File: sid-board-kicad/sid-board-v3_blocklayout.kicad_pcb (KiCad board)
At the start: 2 copper layers, 49 parts, among them J1 SPI + UART, J2 USB_B_Micro, J3 UART, Q1 BSS138, Q2 BSS138, SW1 SW_EN, SW2 SW_FLASH, U1 SC16IS752IPW, U2 MCP1703A-3302_SOT223, U3 SN65HVD232, U4 SN65HVD232, U5 CY7C65213-28PVXI, U6 ESP32-WROOM-32U, U7 SN65HVD232, X1 S53305-24.000-X

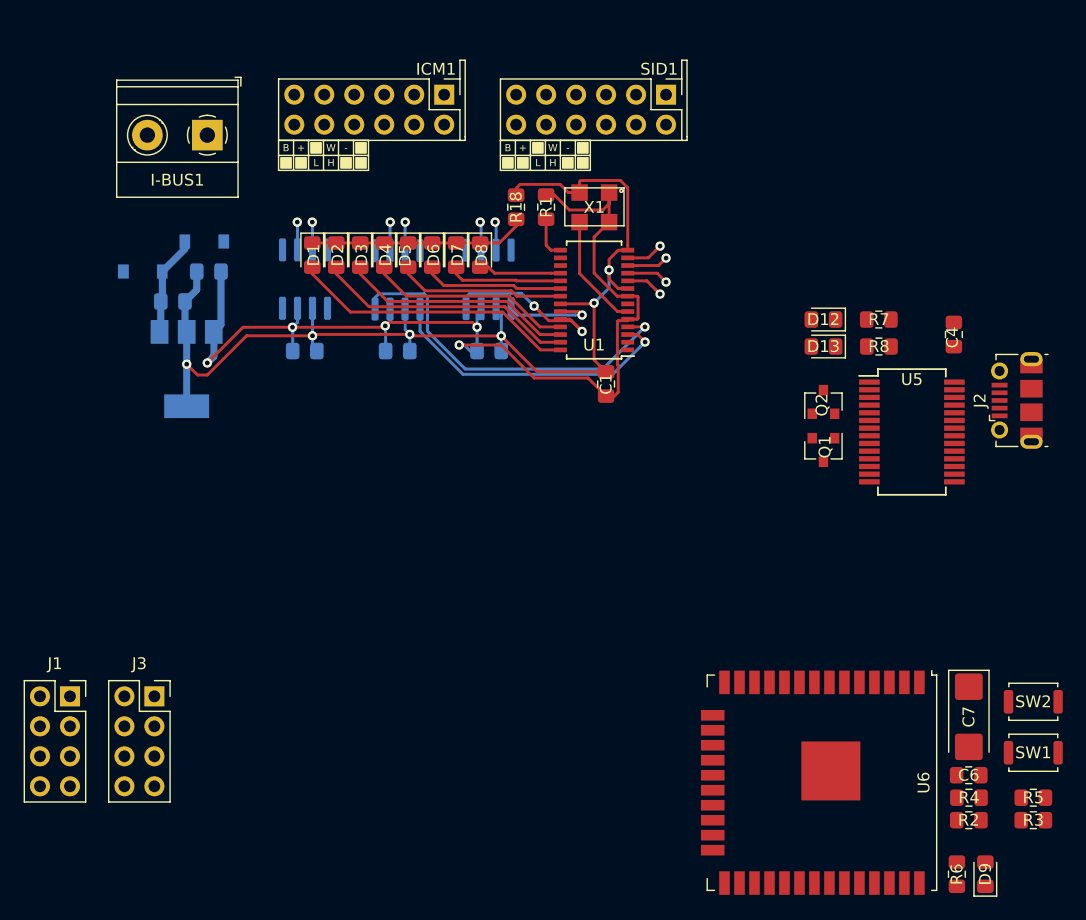
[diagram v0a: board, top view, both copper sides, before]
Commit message: Redid routing more logically
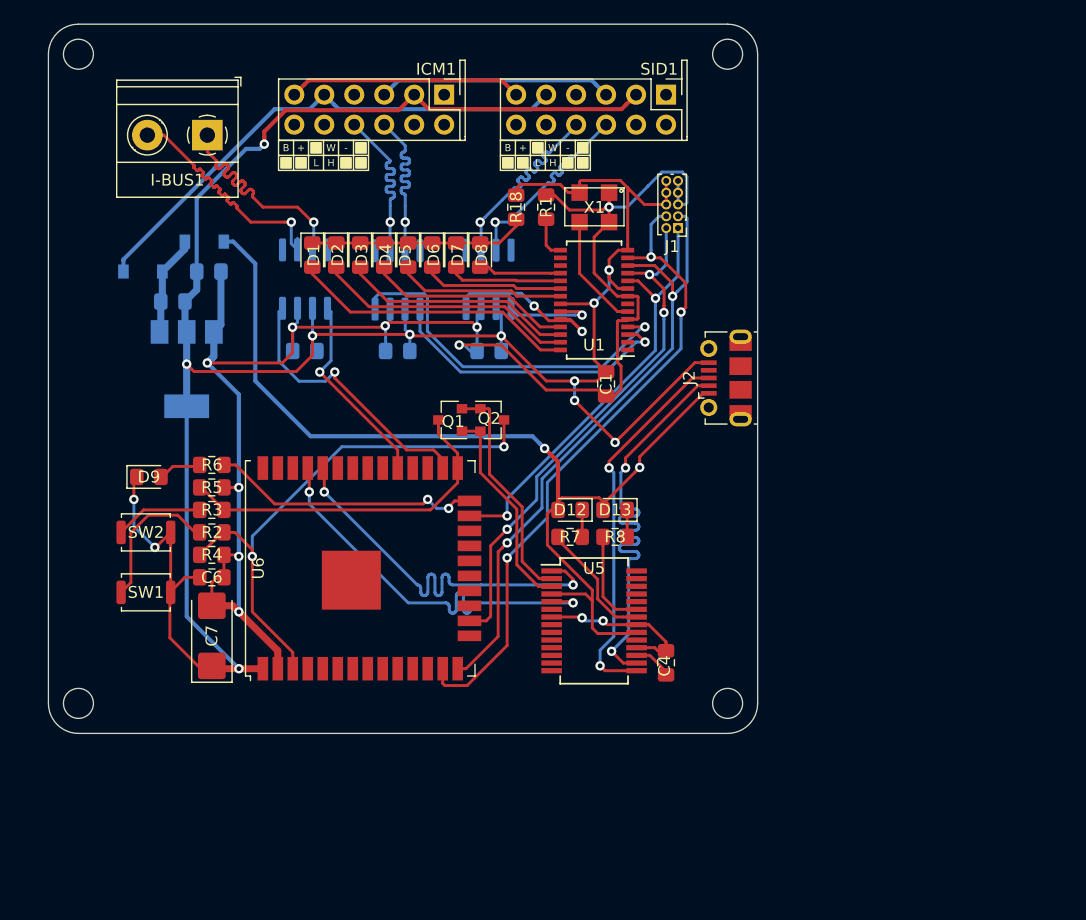
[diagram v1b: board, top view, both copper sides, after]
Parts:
- removed J3: UART, Connector_PinSocket_2.54mm:PinSocket_2x04_P2.54mm_Vertical
- J1: footprint Connector_PinSocket_2.54mm:PinSocket_2x04_P2.54mm_Vertical -> Connector_PinHeader_1.00mm:PinHeader_2x05_P1.00mm_Vertical
- moved D9 78.5 mm to (121.3, 101.6), turned to 0 degrees
- moved SW2 76.5 mm to (121.0, 106.3), turned to 180 degrees
- moved SW1 76.4 mm to (121.0, 111.4), turned to 180 degrees
- moved R3 74.4 mm to (126.6, 104.4), turned to 180 degrees
- moved R5 74.4 mm to (126.6, 102.5)
- moved R6 72.0 mm to (126.6, 100.6), turned to 0 degrees
- moved R2 68.6 mm to (126.6, 106.3), turned to 180 degrees
- moved R4 67.4 mm to (126.6, 108.2)
- moved C6 66.3 mm to (126.6, 110.1), turned to 0 degrees
- moved J1 65.0 mm to (166.1, 80.5), turned to 180 degrees
- moved C7 64.5 mm to (126.6, 115.1), turned to 90 degrees
- moved U6 43.1 mm to (139.2, 109.3), turned to 90 degrees
- moved C4 37.0 mm to (165.1, 117.3)
- moved R7 32.0 mm to (157.0, 106.7), turned to 0 degrees
- moved Q1 31.7 mm to (146.8, 96.8), turned to 180 degrees
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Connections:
- I-BUS1 pad 1: CAN_L -> CAN_H
- I-BUS1 pad 2: CAN_H -> CAN_L
- J1 pad 2: CLK -> MOSI
- J1 pad 3: MOSI -> MISO
- J1 pad 4: MISO -> CLK
- J1 pad 5: GND -> VDD_3.3V
- J1 pad 6: VDD_3.3V -> GND
- J1 pad 7: TXA -> VDD_3.3V
- J1 pad 8: RXA -> GND
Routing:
- net GND: track 96.6 -> 239.5 mm, vias 6 -> 15
- net VBUS: track 0.00 -> 84.7 mm, vias 0 -> 2
- net VDD_3.3V: track 89.7 -> 148.6 mm, vias 5 -> 9
- net CLK: track 3.15 -> 55.3 mm, vias 1 -> 3
- net MISO: track 3.51 -> 53.0 mm, vias 1 -> 2
- net EN: track 0.00 -> 45.8 mm, vias 0 -> 2
- net Net-(D11-Pad2): track 0.00 -> 43.6 mm
- net MOSI: track 3.56 -> 44.3 mm, vias 1 -> 3
- net USB_DM: track 0.00 -> 39.8 mm, vias 0 -> 2
- net RX_ESP32: track 0.00 -> 35.4 mm, vias 0 -> 2
- net TX_ESP32: track 0.00 -> 35.0 mm, vias 0 -> 2
- net CS: track 3.20 -> 36.5 mm, vias 1 -> 2
- net USB_DP: track 0.00 -> 32.6 mm, vias 0 -> 2
- net IO0: track 0.00 -> 29.6 mm
- net RX_ESP32_CAN: track 0.00 -> 23.6 mm, vias 0 -> 1
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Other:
- board outline added: 60.1 x 60.1 mm

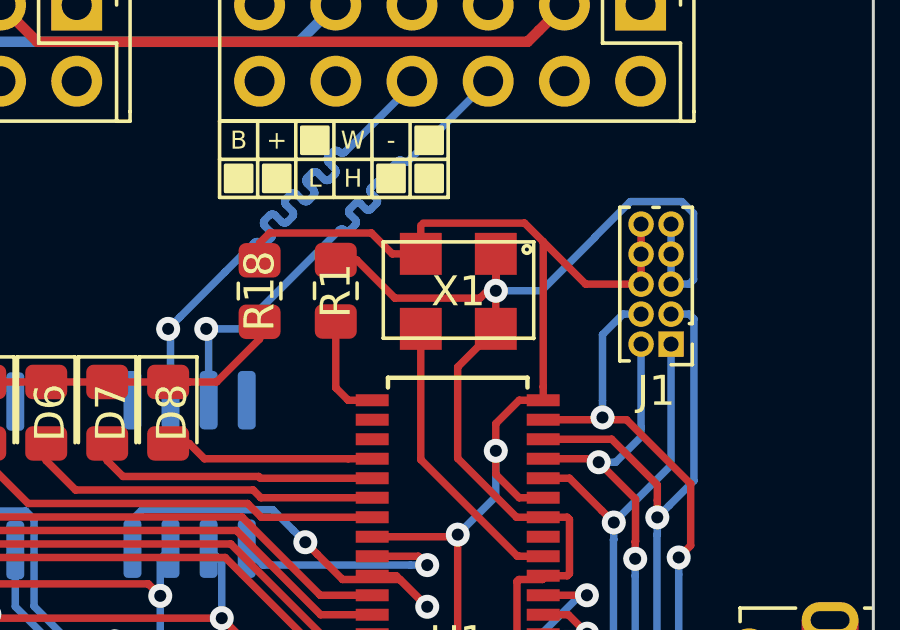
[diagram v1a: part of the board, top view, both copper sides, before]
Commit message: Happy with routing, replaced oscillator, need to label.
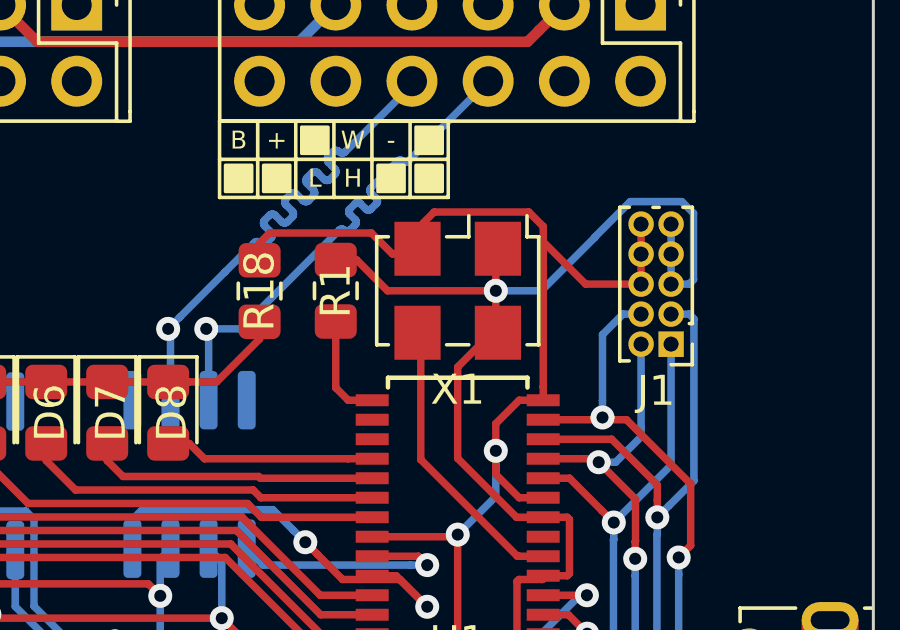
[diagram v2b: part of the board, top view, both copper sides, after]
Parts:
- X1: value S53305-24.000-X -> ASE-xxxMHz; footprint sid-board:S53305-16.000-X -> Oscillator:Oscillator_SMD_EuroQuartz_XO53-4Pin_5.0x3.2mm_HandSoldering
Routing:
- net VDD_3.3V: track 148.6 -> 147.9 mm
- net GND: track 239.5 -> 240.1 mm
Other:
- rule trace_min: 0.2 -> 0.1

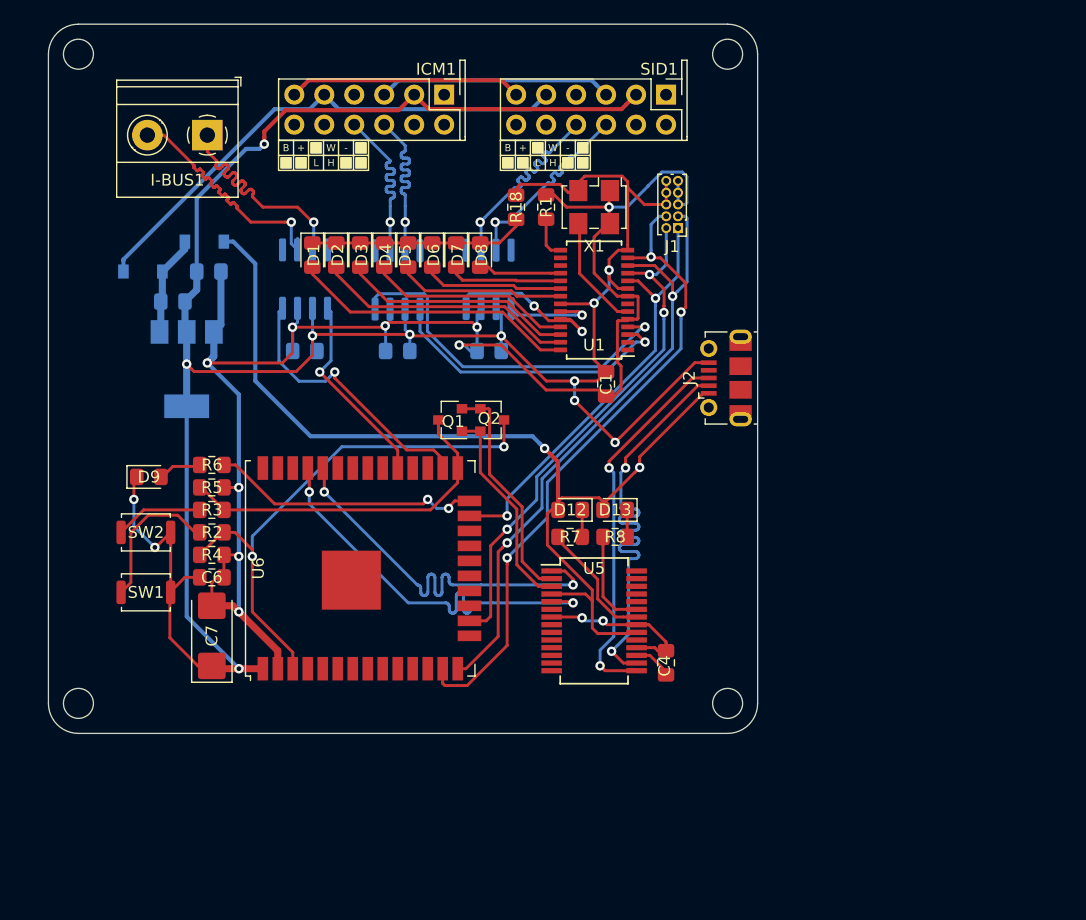
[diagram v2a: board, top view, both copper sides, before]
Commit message: Moved labels
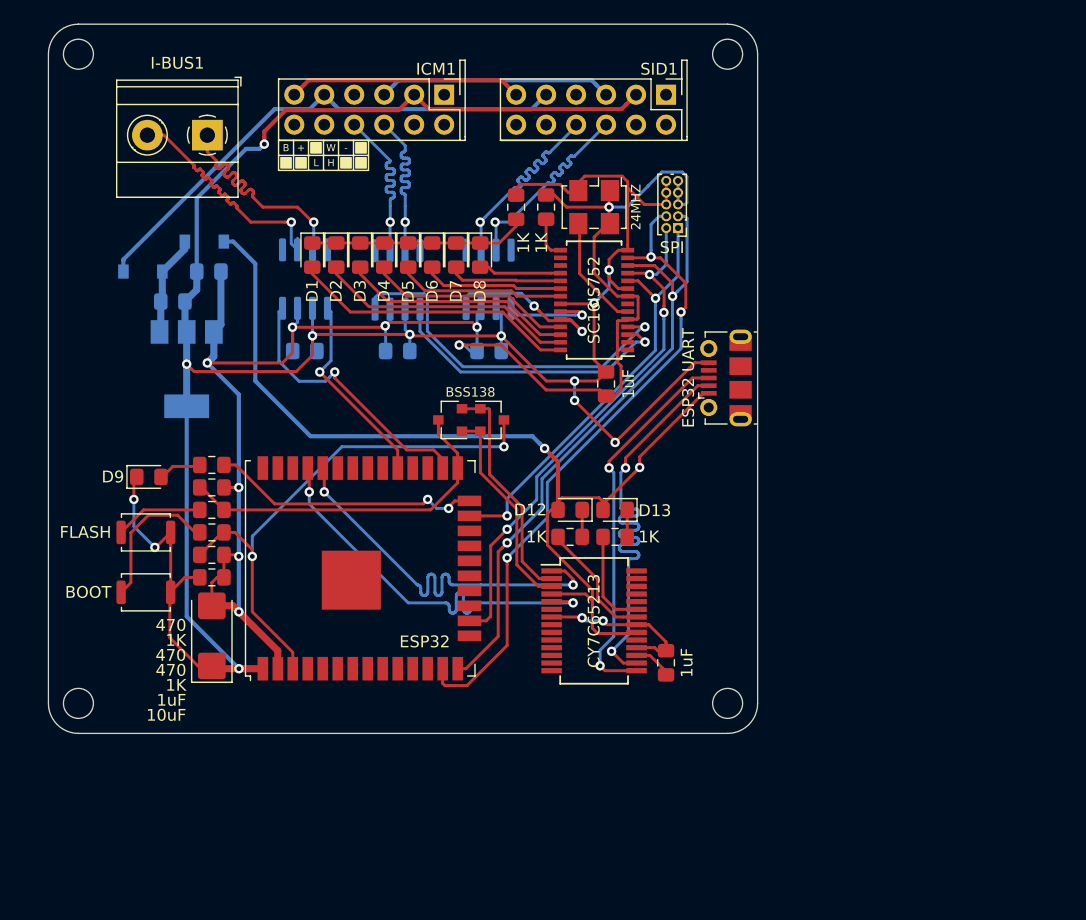
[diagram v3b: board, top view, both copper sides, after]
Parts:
- added ?: , , F.Cu at (123.2, 81.3)
- added ?: , , F.Cu at (121.9, 81.9)
- ESP32 UART: renamed from J2
- U2: value MCP1703A-3302_SOT223 -> MCP1703A-33
- U3: value SN65HVD232 -> SN65HVD232 x3
- renumbered C7 to 10uF, R1 to 1K, R4 to 1K, R7 to 1K, R5 to 1K, R18 to 1K, R8 to 1K, C8 to 1uF, C1 to 1uF, C9 to 1uF, C4 to 1uF, C6 to 1uF, C3 to 1uF, C5 to 1uF, X1 to 24MHZ, R3 to 470, R6 to 470, R2 to 470, SW1 to BOOT, Q2 to BSS138, U5 to CY7C65213, U6 to ESP32, SW2 to FLASH, U1 to SC16IS752, U4 to SN65HVD232, J1 to SPI

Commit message: Added IO expansion for free pins on ESP32
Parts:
- added IO: Conn_01x12, Connector_PinHeader_2.54mm:PinHeader_1x12_P2.54mm_Vertical, F.Cu at (128.9, 121.5)
- J2: renamed from ESP32 UART
- U2: value MCP1703A-33 -> MCP1703A-3302_SOT223
- U3: value SN65HVD232 x3 -> SN65HVD232
- renumbered 1uF to C1, 1uF to C3, 1uF to C4, 1uF to C5, 1uF to C6, 10uF to C7, 1uF to C8, 1uF to C9, SPI to J1, BSS138 to Q2, 1K to R1, 1K to R18, 470 to R2, 470 to R3, 1K to R4, 1K to R5, 470 to R6, 1K to R7, 1K to R8, BOOT to SW1, FLASH to SW2, SC16IS752 to U1, SN65HVD232 to U4, CY7C65213 to U5, ESP32 to U6, 24MHZ to X1
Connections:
- ICM1 pad 1: (no net) -> Net-(ICM1-Pad1)
- ICM1 pad 11: (no net) -> Net-(ICM1-Pad11)
- ICM1 pad 12: (no net) -> Net-(ICM1-Pad12)
- ICM1 pad 4: (no net) -> Net-(ICM1-Pad4)
- ICM1 pad 7: (no net) -> Net-(ICM1-Pad7)
- ICM1 pad 8: (no net) -> Net-(ICM1-Pad8)
- J2 pad 4: (no net) -> Net-(J2-Pad4)
- SID1 pad 1: (no net) -> Net-(SID1-Pad1)
- SID1 pad 11: (no net) -> Net-(SID1-Pad11)
- SID1 pad 12: (no net) -> Net-(SID1-Pad12)
- SID1 pad 4: (no net) -> Net-(SID1-Pad4)
- SID1 pad 7: (no net) -> Net-(SID1-Pad7)
- SID1 pad 8: (no net) -> Net-(SID1-Pad8)
- U1 pad 1: (no net) -> Net-(U1-Pad1)
- U1 pad 16: (no net) -> Net-(U1-Pad16)
- U1 pad 17: (no net) -> Net-(U1-Pad17)
- U1 pad 2: (no net) -> Net-(U1-Pad2)
- U1 pad 7: (no net) -> Net-(U1-Pad7)
- U3 pad 5: (no net) -> Net-(U3-Pad5)
- U3 pad 8: (no net) -> Net-(U3-Pad8)
- U4 pad 5: (no net) -> Net-(U4-Pad5)
- U4 pad 8: (no net) -> Net-(U4-Pad8)
- U5 pad 10: (no net) -> Net-(U5-Pad10)
- U5 pad 11: (no net) -> Net-(U5-Pad11)
- U5 pad 12: (no net) -> Net-(U5-Pad12)
- U5 pad 13: (no net) -> Net-(U5-Pad13)
- U5 pad 14: (no net) -> Net-(U5-Pad14)
- U5 pad 19: (no net) -> Net-(U5-Pad19)
- U5 pad 24: (no net) -> Net-(U5-Pad24)
- U5 pad 25: (no net) -> Net-(U5-Pad25)
- U5 pad 26: (no net) -> Net-(U5-Pad26)
- U5 pad 27: (no net) -> Net-(U5-Pad27)
- U5 pad 28: (no net) -> Net-(U5-Pad28)
- U5 pad 6: (no net) -> Net-(U5-Pad6)
- U5 pad 8: (no net) -> Net-(U5-Pad8)
- U5 pad 9: (no net) -> Net-(U5-Pad9)
- U6 pad 10: (no net) -> Net-(J3-Pad10)
- U6 pad 11: (no net) -> Net-(J3-Pad11)
- U6 pad 12: (no net) -> Net-(J3-Pad12)
- U6 pad 17: (no net) -> Net-(U6-Pad17)
- U6 pad 18: (no net) -> Net-(U6-Pad18)
- U6 pad 19: (no net) -> Net-(U6-Pad19)
- U6 pad 20: (no net) -> Net-(U6-Pad20)
- U6 pad 21: (no net) -> Net-(U6-Pad21)
- U6 pad 22: (no net) -> Net-(U6-Pad22)
- U6 pad 27: (no net) -> Net-(U6-Pad27)
- U6 pad 28: (no net) -> Net-(U6-Pad28)
- U6 pad 30: (no net) -> Net-(U6-Pad30)
- U6 pad 31: (no net) -> Net-(U6-Pad31)
- U6 pad 32: (no net) -> Net-(U6-Pad32)
- U6 pad 33: (no net) -> Net-(U6-Pad33)
- U6 pad 36: (no net) -> Net-(U6-Pad36)
- U6 pad 37: (no net) -> Net-(U6-Pad37)
- U6 pad 4: (no net) -> Net-(J3-Pad4)
- U6 pad 5: (no net) -> Net-(J3-Pad5)
- U6 pad 6: (no net) -> Net-(J3-Pad6)
- U6 pad 7: (no net) -> Net-(J3-Pad7)
- U6 pad 8: (no net) -> Net-(J3-Pad8)
- U6 pad 9: (no net) -> Net-(J3-Pad9)
- U7 pad 5: (no net) -> Net-(U7-Pad5)
- U7 pad 8: (no net) -> Net-(U7-Pad8)
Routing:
- net Net-(J3-Pad12): track 0.00 -> 18.0 mm, vias 0 -> 1
- net Net-(J3-Pad11): track 0.00 -> 16.3 mm, vias 0 -> 1
- net Net-(J3-Pad10): track 0.00 -> 14.7 mm, vias 0 -> 1
- net Net-(J3-Pad9): track 0.00 -> 13.1 mm, vias 0 -> 1
- net Net-(J3-Pad8): track 0.00 -> 8.84 mm
- net Net-(J3-Pad7): track 0.00 -> 7.57 mm
- net Net-(J3-Pad6): track 0.00 -> 6.30 mm
- net GND: track 240.1 -> 245.4 mm
- net Net-(J3-Pad5): track 0.00 -> 4.95 mm
- net Net-(J3-Pad4): track 0.00 -> 4.43 mm
- net VDD_3.3V: track 147.9 -> 151.9 mm
